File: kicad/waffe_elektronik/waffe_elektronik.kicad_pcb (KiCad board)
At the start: 4 copper layers, 59.6 x 46 mm, 63 parts, among them J1 WS2812 HP-Streifen, J2 GX16 7-polig, J3 USB-C (Flashen + Laden), J4 OLED I²C (Qwiic), J5 Drehgeber, J6 TSOP 6 (Waffe), M1 Vibromotor, Q1 AO3400A, Q2 AO3400A, SW1 Taster, SW2 Taster, SW3 RESET, SW4 BOOT, U1 MT3608, U12 USBLC6-2SC6, U2 AMS1117-3.3, U3 MCP73831, U4 ESP32-S3-WROOM-1-N16R8, U5 74HCT125, U6 MAX98357A

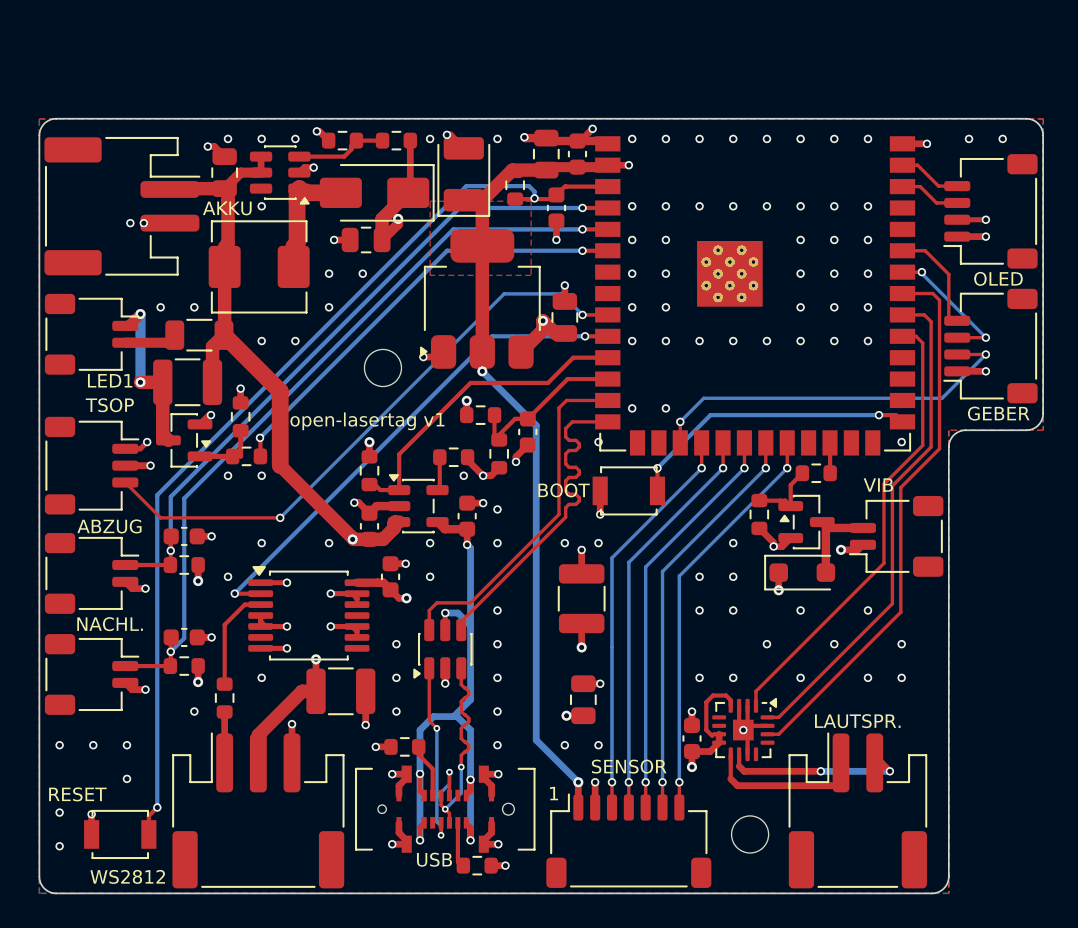
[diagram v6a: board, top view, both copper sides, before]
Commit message: Platine: Stecker nach Kabelwegen ausgerichtet, USB-C bündig mit der Gehäusewand
J1/SP1 an die linke Kante (Hauptschacht), SW1/SW2 an die Unterkante (Kanal zum
Abzugsschalter), J2 rechts unter M1 (Motorschacht), RESET auf den EN-Weg.
USB-C hanxia HX-TYPE-C 16P 180 LT H10.5 (10,5 mm), neues USB-Routing, Paar gleich lang.
J1 auf CJT A2001WR-S-3P (Lager). Gehäuse: Zonen, USB-Durchbruch mit Mulde,
Nachladetaste 5 mm nach hinten. Kabelwege, Fertigungsdaten, Bilder, READMEs neu.
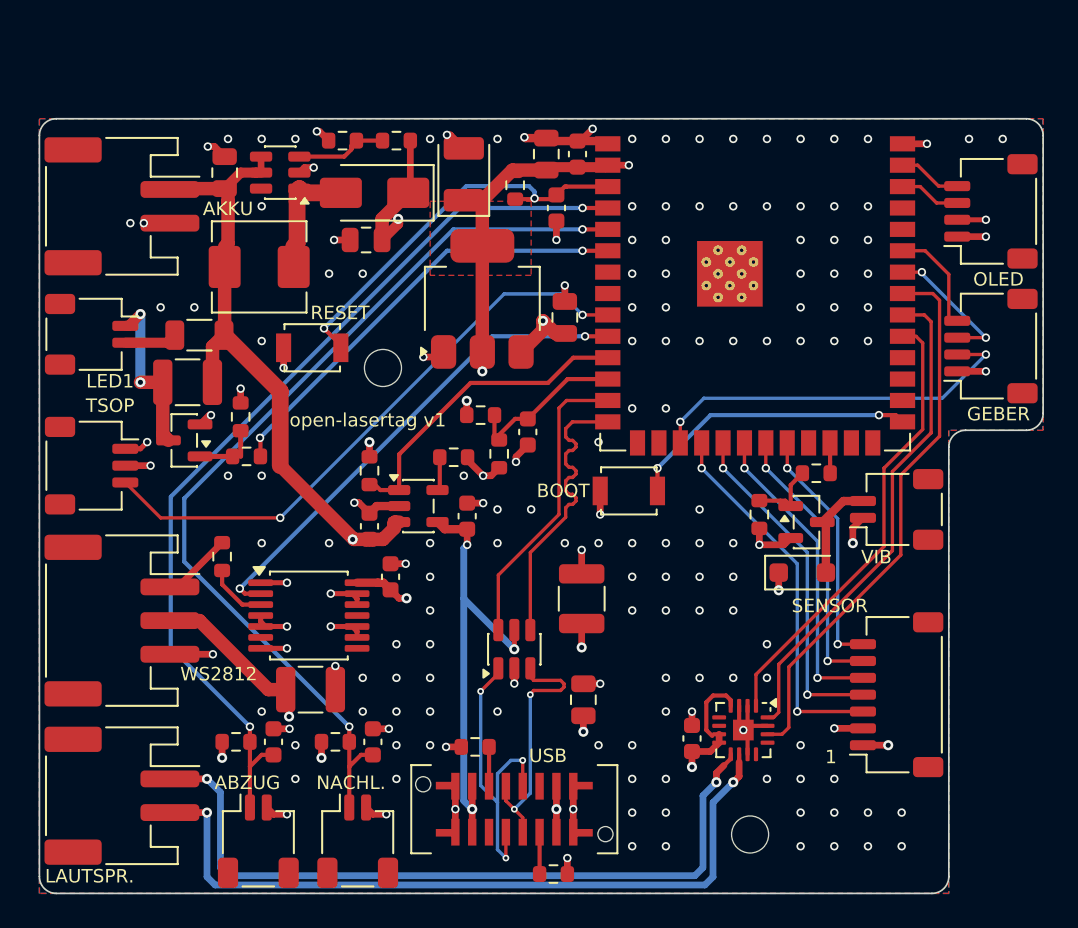
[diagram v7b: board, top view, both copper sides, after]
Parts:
- J3: footprint lasertag:USB_C_Receptacle_HRO_TYPE-C-31-E-17_Vertical -> lasertag:USB_C_Receptacle_HX_TYPE-C-16P-180-LT-H10.5_Vertical
- moved SP1 43.7 mm to (4.90, 40.2), turned to -90 degrees
- moved SW3 31.1 mm to (16.2, 13.6)
- moved SW1 18.7 mm to (13.0, 42.9), turned to 0 degrees
- moved SW2 18.6 mm to (18.9, 42.9), turned to 0 degrees
- moved J2 18.1 mm to (50.9, 34.2), turned to 90 degrees
- moved J1 13.9 mm to (4.90, 29.8), turned to -90 degrees
- moved C8 13.3 mm to (13.9, 37.0), turned to 90 degrees
- moved C9 12.8 mm to (19.8, 37.0), turned to 90 degrees
- moved R9 10.9 mm to (11.7, 37.0), turned to 0 degrees
- moved R10 10.0 mm to (17.6, 37.0), turned to 0 degrees
- moved R15 8.40 mm to (10.8, 26.0), turned to 90 degrees
- moved R22 4.55 mm to (30.5, 44.9)
- moved R23 4.18 mm to (25.9, 37.3)
- moved J3 4.10 mm to (28.2, 41.0)
- moved U12 4.10 mm to (28.2, 31.5)
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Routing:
- net Net-(U6-OUTP): track 7.93 -> 44.3 mm, vias 0 -> 2
- net Net-(U6-OUTN): track 10.9 -> 44.4 mm
- net Net-(U4-EN): track 56.7 -> 23.9 mm
- net 3V3_MCU: track 114.6 -> 134.3 mm
- net /TRIGGER: track 40.6 -> 55.1 mm
- net /RELOAD: track 45.6 -> 55.9 mm
- net /TSOP5_OUT: track 24.3 -> 14.7 mm
- net /TSOP4_OUT: track 24.2 -> 16.6 mm
- net 5V_PERIPH: track 113.3 -> 120.1 mm
- net /TSOP3_OUT: track 24.1 -> 18.4 mm
- net Net-(J3-D--PadA7): track 14.1 -> 18.9 mm
- net /TSOP2_OUT: track 24.0 -> 20.3 mm
- net Net-(J3-D+-PadA6): track 11.9 -> 15.4 mm
- net /USB_D+: track 20.6 -> 17.8 mm
- net /USB_D-: track 20.6 -> 17.8 mm
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
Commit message: Platine: Flash 128 MB, microSD-Slot, Akkuschutz; Schaltplan auf fünf Seiten
- SPI-NAND GD5F1GQ5UEYIGR (U14, 128 MB) für Audio-Dateien an IO7/IO15/IO3/IO46
- microSD-Slot TF-018 (J7, Push-Pull) am selben SPI-Bus, /CS an IO48, DAT1/DAT2 mit Pull-up
- Akkuschutz DW01A + FS8205A in einer Lasche oben links neben BT1
- USB versorgt 5V_PERIPH über SS14 (Flashen ohne Akku), STAT über BAT54WS an IO18
- C7 als IR-Puffer an GND, TSOP-Leitungen über 100 Ω an J2
- Platine 59,6 × 51 mm, J2 an der rechten Kante, H2 versetzt, Gehäusetasche und Kabelwege angepasst
- Schaltplan hierarchisch: Übersicht + fünf A3-Seiten, Projekt-Symbolbibliothek, ERC ohne Meldungen
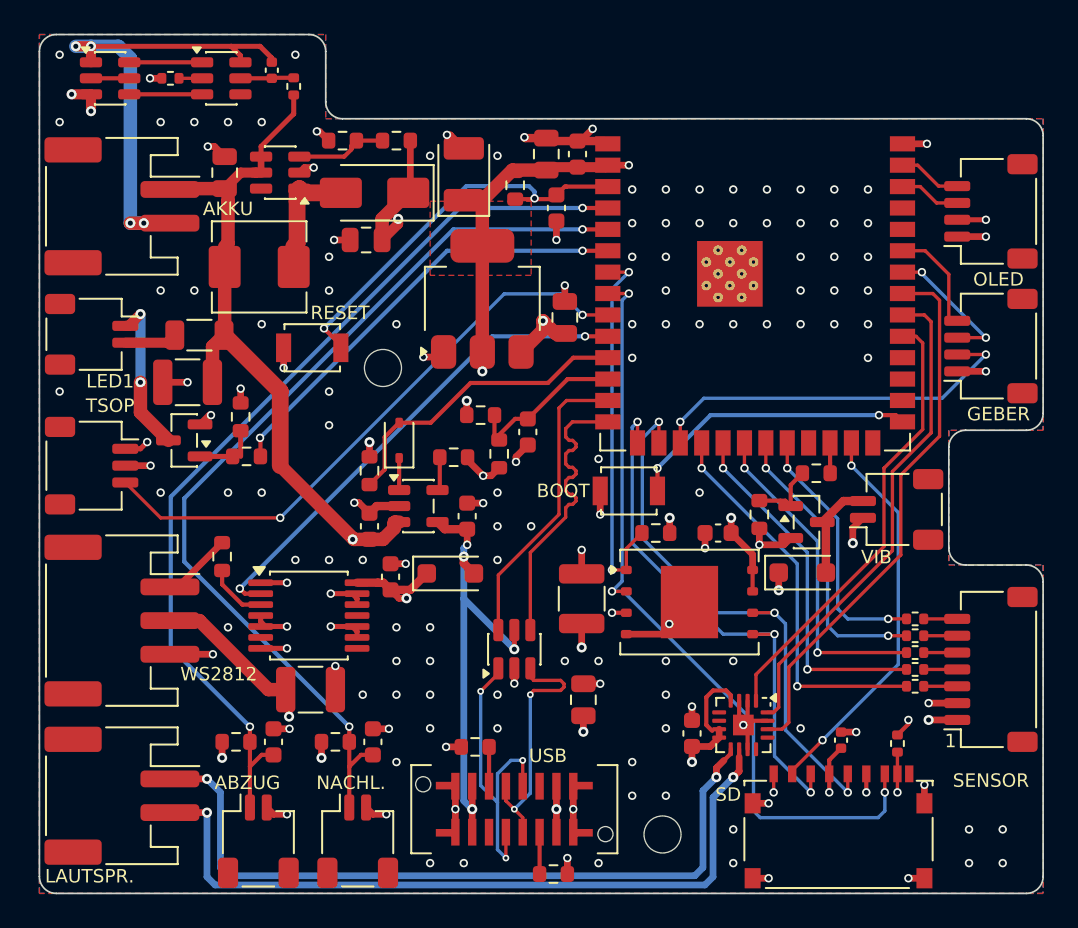
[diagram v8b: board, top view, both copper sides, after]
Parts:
- added C25: 100n, Capacitor_SMD:C_0603_1608Metric, F.Cu at (40.3, 24.6)
- added C26: 100n, Capacitor_SMD:C_0402_1005Metric, F.Cu at (47.6, 36.9)
- added C27: 100n, Capacitor_SMD:C_0402_1005Metric, F.Cu at (13.8, -2.88)
- added D4: SS14, Diode_SMD:D_SOD-123F, F.Cu at (24.4, 27.0)
- added D5: BAT54WS, Diode_SMD:D_SOD-323, F.Cu at (21.4, 19.1)
- added J7: TF-018, lasertag:microSD_TF-018_PushPull, F.Cu at (47.5, 42.0)
- added Q3: FS8205A, Package_TO_SOT_SMD:SOT-23-6, F.Cu at (4.20, -2.40)
- added R27: 10k, Resistor_SMD:R_0603_1608Metric, F.Cu at (36.6, 24.6)
- added R28: 100, Resistor_SMD:R_0402_1005Metric, F.Cu at (15.1, -1.92)
- added R29: 1k, Resistor_SMD:R_0402_1005Metric, F.Cu at (7.78, -2.40)
- added R30: 100, Resistor_SMD:R_0402_1005Metric, F.Cu at (52.0, 33.7)
- added R31: 100, Resistor_SMD:R_0402_1005Metric, F.Cu at (52.0, 32.7)
- added R32: 100, Resistor_SMD:R_0402_1005Metric, F.Cu at (52.0, 31.7)
- added R33: 100, Resistor_SMD:R_0402_1005Metric, F.Cu at (52.0, 30.7)
- added R34: 100, Resistor_SMD:R_0402_1005Metric, F.Cu at (52.0, 29.7)
- added R37: 10k, Resistor_SMD:R_0402_1005Metric, F.Cu at (51.0, 37.1)
- added U14: GD5F1GQ5UEYIGR, Package_SON:WSON-8-1EP_8x6mm_P1.27mm_EP3.4x4.3mm, F.Cu at (38.6, 28.7)
- added U15: DW01A, Package_TO_SOT_SMD:SOT-23-6, F.Cu at (10.8, -2.40)
- moved J2 5.80 mm to (56.5, 32.7)
- moved H2 5.20 mm to (37.0, 42.5)
- moved C23 0.30 mm to (38.8, 36.5)
- moved U6 0.30 mm to (41.8, 36.0)
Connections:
- net /ADC_BATT renamed ADC_BATT
- net /ENC_A renamed ENC_A
- net /ENC_B renamed ENC_B
- net /ENC_SW renamed ENC_SW
- net /I2C_SCL renamed I2C_SCL
- net /I2C_SDA renamed I2C_SDA
- net /I2S_BCLK renamed I2S_BCLK
- net /I2S_DOUT renamed I2S_DOUT
- net /I2S_LRCLK renamed I2S_LRCLK
- net /IR_GATE renamed IR_GATE
- net /RELOAD renamed RELOAD
- net /TRIGGER renamed TRIGGER
- net /TSOP6_OUT renamed TSOP6_OUT
- net /USB_D+ renamed USB_D+
- net /USB_D- renamed USB_D-
- net /VIB renamed VIB
- net /WS2812_DIN_3V3 renamed WS2812_DIN_3V3
- BT1 pad 2: GND -> BAT_N
- C7 pad 2: Net-(LED1-K) -> GND
- J2 pad 3: /TSOP1_OUT -> TSOP1_J
- J2 pad 4: /TSOP2_OUT -> TSOP2_J
- J2 pad 5: /TSOP3_OUT -> TSOP3_J
- J2 pad 6: /TSOP4_OUT -> TSOP4_J
- J2 pad 7: /TSOP5_OUT -> TSOP5_J
- R2 pad 2: /CHRG_STAT -> CHRG_STAT
- U3 pad 1: /CHRG_STAT -> Net-(D5-K)
- U4 pad 11: /CHRG_STAT -> CHRG_STAT
- U4 pad 15: unconnected-(U4-IO3-Pad15) -> SPI_MOSI
- U4 pad 16: unconnected-(U4-IO46-Pad16) -> SPI_CLK
- U4 pad 18: /TSOP1_OUT -> TSOP1_OUT
- U4 pad 19: /TSOP2_OUT -> TSOP2_OUT
- U4 pad 20: /TSOP3_OUT -> TSOP3_OUT
- U4 pad 21: /TSOP4_OUT -> TSOP4_OUT
- U4 pad 22: /TSOP5_OUT -> TSOP5_OUT
- U4 pad 25: unconnected-(U4-IO48-Pad25) -> SD_CS
- U4 pad 7: unconnected-(U4-IO7-Pad7) -> FLASH_CS
- U4 pad 8: unconnected-(U4-IO15-Pad8) -> SPI_MISO
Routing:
- net SPI_MISO: track 0.00 -> 47.4 mm, vias 0 -> 3
- net 3V3_MCU: track 134.3 -> 172.9 mm, vias 8 -> 13
- net SPI_CLK: track 0.00 -> 33.1 mm, vias 0 -> 3
- net SPI_MOSI: track 0.00 -> 32.0 mm, vias 0 -> 3
- net BAT_N: track 0.00 -> 30.8 mm, vias 0 -> 4
- net SD_CS: track 0.00 -> 23.4 mm, vias 0 -> 2
- net TSOP1_OUT: track 0.00 -> 23.3 mm, vias 0 -> 2
- net FLASH_CS: track 0.00 -> 22.8 mm, vias 0 -> 2
- net /TSOP1_OUT: track 22.2 -> 0.00 mm, vias 2 -> 0
- net TSOP2_OUT: track 0.00 -> 21.4 mm, vias 0 -> 2
- net /TSOP2_OUT: track 20.3 -> 0.00 mm, vias 2 -> 0
- net TSOP3_OUT: track 0.00 -> 19.5 mm, vias 0 -> 2
- net /CHRG_STAT: track 18.8 -> 0.00 mm
- net /TSOP3_OUT: track 18.4 -> 0.00 mm, vias 2 -> 0
- net CHRG_STAT: track 0.00 -> 18.4 mm
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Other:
- board size 59.6 x 46 mm -> 59.6 x 51 mm
- board text added: "SD"
